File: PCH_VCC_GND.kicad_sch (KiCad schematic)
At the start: 1 part

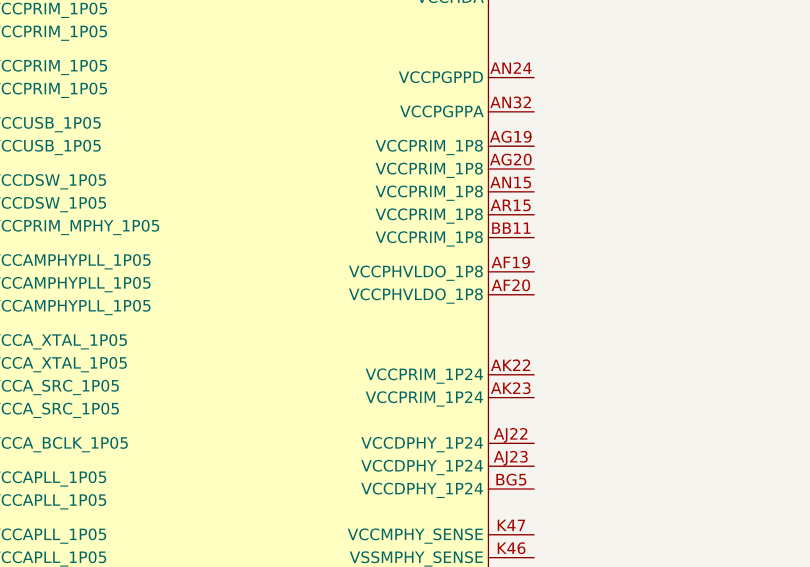
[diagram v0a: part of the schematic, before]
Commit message: Added PCH PCIe rootport/bifurcation notes
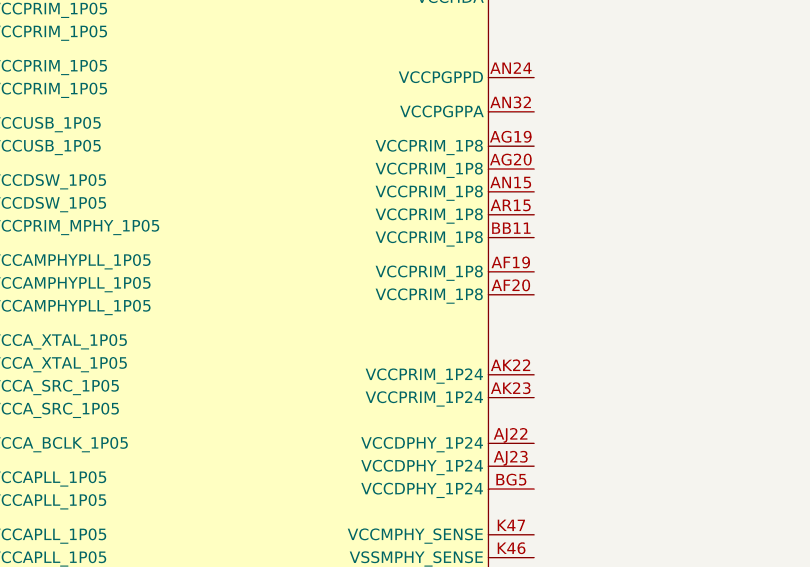
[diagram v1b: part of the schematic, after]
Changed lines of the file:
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@@
 	)
 	(symbol
+		(lib_name "Intel_CFL_PCH_FCBGA874_but_better_2")
 		(lib_id "A-my-stuff:Intel_CFL_PCH_FCBGA874_but_better")
 		(at 334.01 63.5 0)
@@
 					(unit 12)
 				)
+				(path "/4bc771b8-eb19-46d0-8798-27231a7c6e83/55a4f655-ea62-4675-bc34-60bbcfd07a2f"
+					(reference "UPCH1")
+					(unit 12)
+				)
 			)
 		)
@@
 					(unit 9)
 				)
+				(path "/4bc771b8-eb19-46d0-8798-27231a7c6e83/55a4f655-ea62-4675-bc34-60bbcfd07a2f"
+					(reference "UPCH1")
+					(unit 9)
+				)
 			)
 		)
@@
 		(pin "G2"
 		)
-		(pin "AL37"
-		)
-		(pin "AN35"
-		)
 		(instances
 			(project "Stroopwafel-LGA1151-CFL"
@@
 					(reference "UPCH1")
 					(unit 8)
+				)
+				(path "/4bc771b8-eb19-46d0-8798-27231a7c6e83/55a4f655-ea62-4675-bc34-60bbcfd07a2f"
+					(reference "UPCH1")
+					(unit 8)
